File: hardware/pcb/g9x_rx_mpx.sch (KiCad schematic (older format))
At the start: 31 parts, among them IC1 ATMEGA328-M, K1 CONN_3, K2 CONN_3, K3 CONN_3, P1 CONN_3X2, P2 CONN_8X3, P3 CONN_8X2, SW1 SPDT_SW, SW2 SPDT_SW, U1 7805, U2 ULN2803, U3 4017_GRUVIN

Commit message: Couple of pin changes to the Rx deMUX board
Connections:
- wire segments 180 -> 178
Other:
- moved on the sheet: C1, C2, C3, C4, C5, C6, C7, C8, C9, IC1, K1, K2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

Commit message: Rx DEMUX board getting closer . Tidied up the schematic . Added fuses . Via-ed the GND pours . Tidied the silkscreen . Also have some working code for testing the hardware PPM decode and encode
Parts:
- added F1, F2: FUSE, symbol FUSE
- added P4: CONN_4, symbol CONN_4
- added P5, P6: CONN_1, symbol CONN_1
- added R11: 4.7k, symbol R
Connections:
- net labels added: RXD, TXD
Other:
- moved on the sheet: P3, U2

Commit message: Rx MPX - Changed switch types (cheaper and better spec), moved fuses. Still want to add a couple of dip switches and an LED for user config options. Then it's done.
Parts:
- removed SW1, SW2: SPDT_SW, symbol SPDT_SW
- added SW1, SW2: SPDT_SW_PCB, symbol SPDT_SW_PCB
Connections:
- wire segments 178 -> 184
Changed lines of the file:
@@
-EESchema Schematic File Version 2  date 02/11/2011 19:17:17
+EESchema Schematic File Version 2  date 15/02/2012 11:27:38
 LIBS:device
 LIBS:transistors
@@
 Sheet 1 1
 Title "G9X Rx Multiplexer Board"
-Date "2 nov 2011"
+Date "15 feb 2012"
 Rev "1.0"
 Comp "gruvin9x"
@@
 Comment4 "Licensed under the TAPR Open Hardware License (see file,  LICENSE)"
 $EndDescr
+Connection ~ 10050 9350
+Wire Wire Line
+	10050 9550 10050 9150
+Wire Wire Line
+	10050 9150 10200 9150
+Connection ~ 9950 2200
+Wire Wire Line
+	10100 2000 9950 2000
+Wire Wire Line
+	9950 2000 9950 2350
 Connection ~ 7750 5450
 Wire Wire Line
@@
 Wire Wire Line
 	7750 4300 7750 4800
+Wire Wire Line
+	9950 2200 10100 2200
+Wire Wire Line
+	10050 9350 10200 9350
+$Comp
+L GND #PWR?
+U 1 1 4F3B9583
+P 10050 9550
+F 0 "#PWR?" H 10050 9550 30  0001 C CNN
+F 1 "GND" H 10050 9480 30  0001 C CNN
+	1    10050 9550
+	1    0    0    -1
+$EndComp
+$Comp
+L GND #PWR?
+U 1 1 4F3B9567
+P 9950 2350
+F 0 "#PWR?" H 9950 2350 30  0001 C CNN
+F 1 "GND" H 9950 2280 30  0001 C CNN
+	1    9950 2350
+	1    0    0    -1
+$EndComp
+$Comp
+L SPDT_SW_PCB SW2
+U 1 1 4F3B8BE9
+P 10700 9050
+F 0 "SW2" H 10500 9400 50  0000 C CNN
+F 1 "SPDT_SW_PCB" H 11000 9500 50  0000 C CNN
+	1    10700 9050
+	-1   0    0    -1
+$EndComp
+$Comp
+L SPDT_SW_PCB SW1
+U 1 1 4F3B8BE1
+P 10600 1900
+F 0 "SW1" H 10400 2250 50  0000 C CNN
+F 1 "SPDT_SW_PCB" H 10900 2350 50  0000 C CNN
+	1    10600 1900
+	-1   0    0    -1
+$EndComp
 $Comp
 L R R11
@@
 Text Label 11050 9450 0    60   ~ 0
 AUX_BATT_2
-Text Label 9750 8750 0    60   ~ 0
+Text Label 9750 8950 0    60   ~ 0
 AUX_BATT_2
 Text Label 9600 1600 0    60   ~ 0
@@
 Text Label 7150 2800 0    60   ~ 0
 SPI_MISO
-Text Label 9750 8950 0    60   ~ 0
+Text Label 9750 8750 0    60   ~ 0
 BATT_RX
 Text Label 9600 1800 0    60   ~ 0
 BATT_RX
 $Comp
-L SPDT_SW SW2
-U 1 1 4EA0A57B
-P 10700 8650
-F 0 "SW2" H 10500 9000 50  0000 C CNN
-F 1 "SPDT_SW" H 11000 9100 50  0000 C CNN
-	1    10700 8650
-	-1   0    0    1
-$EndComp
-$Comp
-L SPDT_SW SW1
-U 1 1 4EA0A572
-P 10600 1900
-F 0 "SW1" H 10400 2250 50  0000 C CNN
-F 1 "SPDT_SW" H 10900 2350 50  0000 C CNN
-	1    10600 1900
-	-1   0    0    -1
-$EndComp
-$Comp
 L CONN_3X2 P1

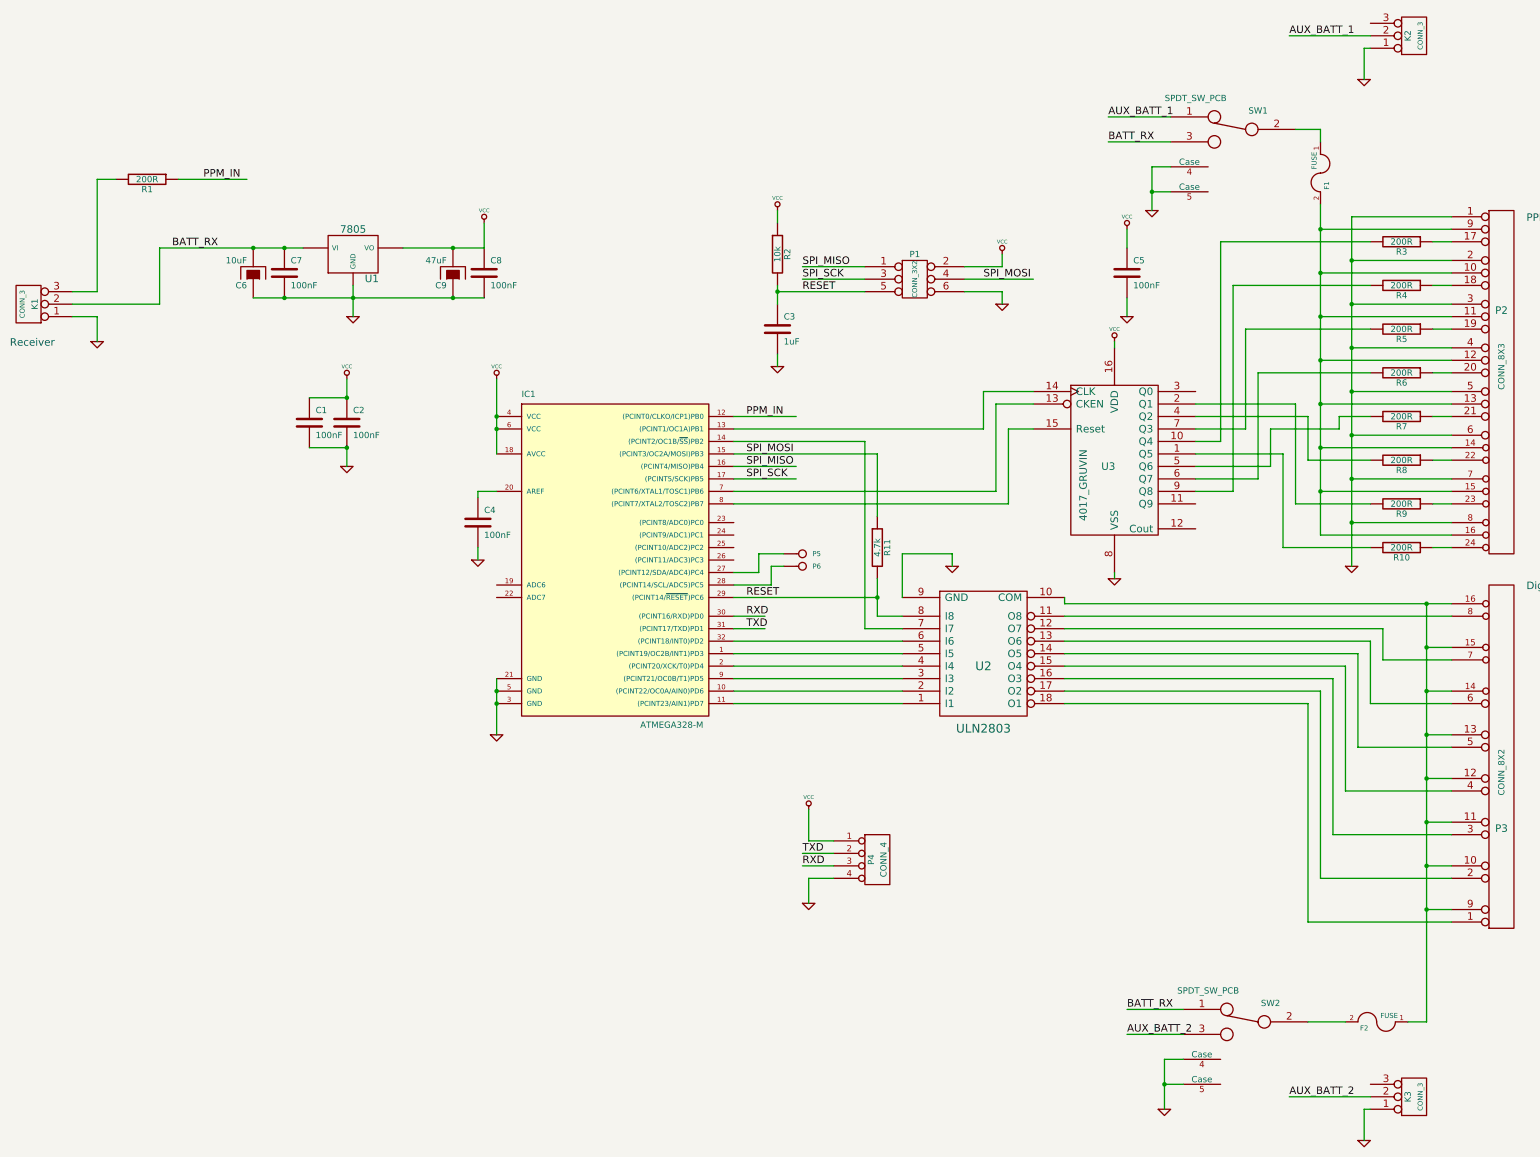
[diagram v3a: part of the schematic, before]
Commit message: Rx MPX board - added LED and dip switches. LED needs attention, no 3D model. Also via search needs to occur.
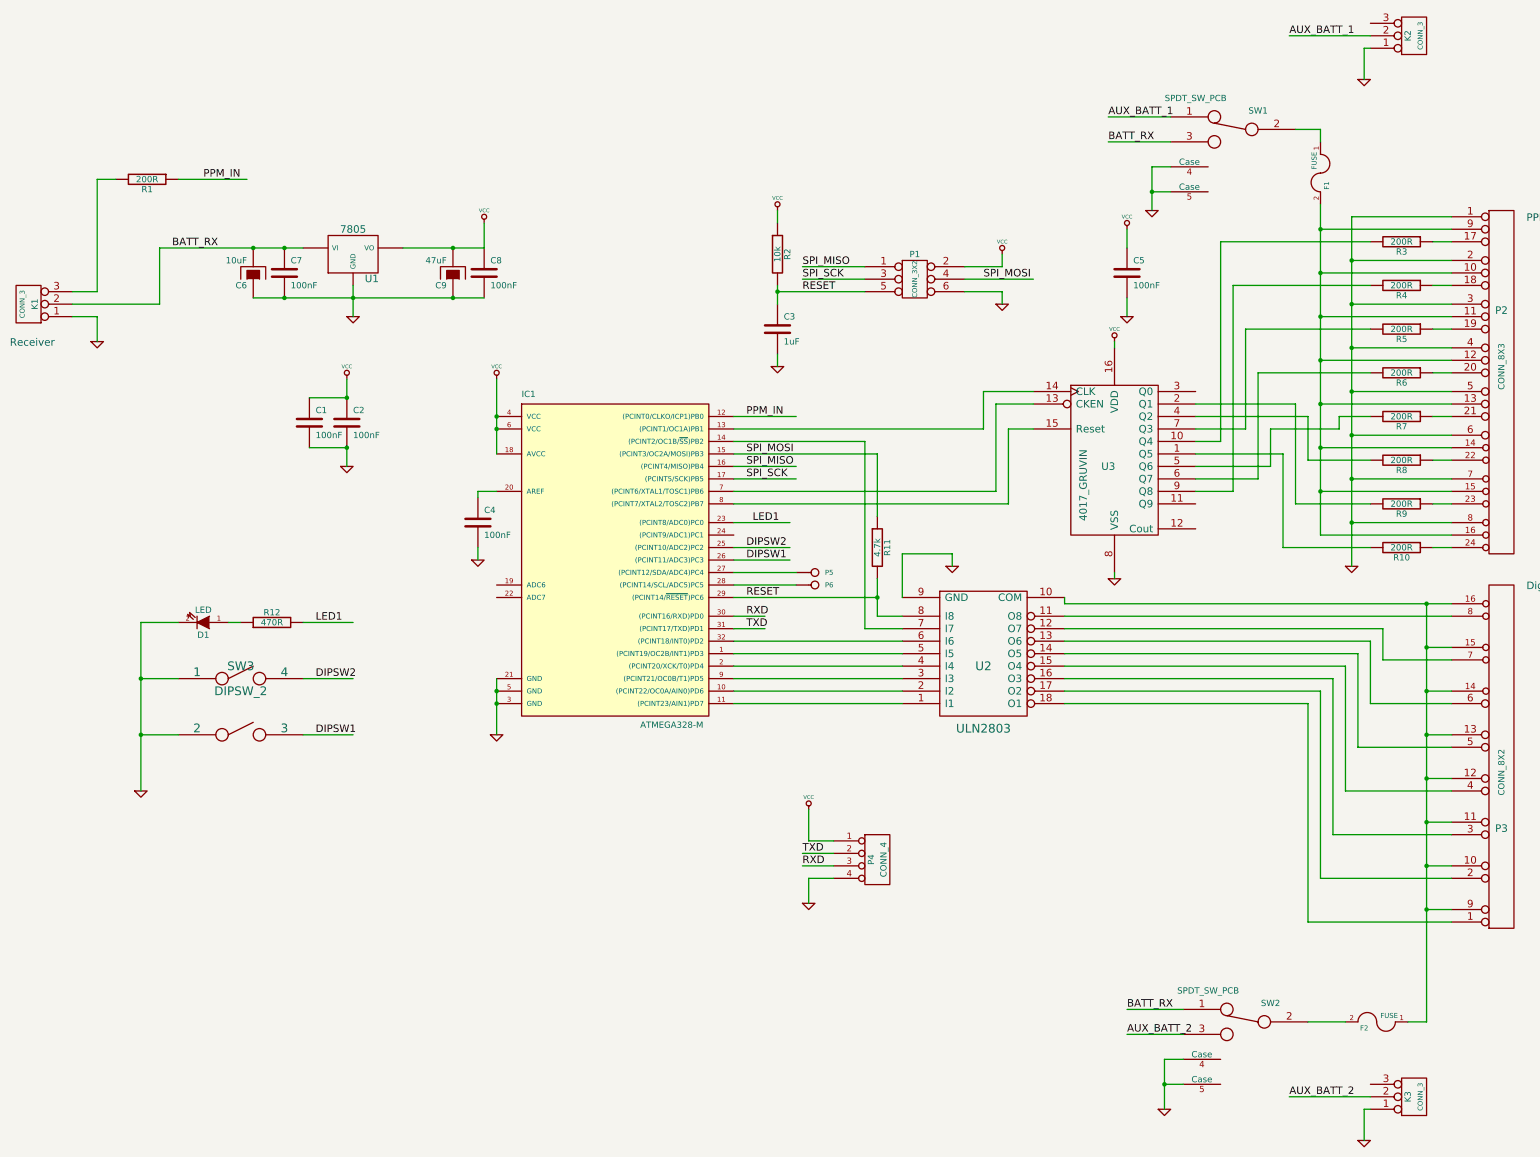
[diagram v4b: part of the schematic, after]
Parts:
- added D1: LED, symbol LED
- added R12: 470R, symbol R
- added SW3: DIPSW_2, symbol DIPSW_2
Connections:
- net labels added: DIPSW1, DIPSW2, LED1
- wire segments 184 -> 191
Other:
- moved on the sheet: P5, P6

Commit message: Rx MPX - Final changes, two regulator alternatives. Next step order them. Bed now, gerbers tomorrow !
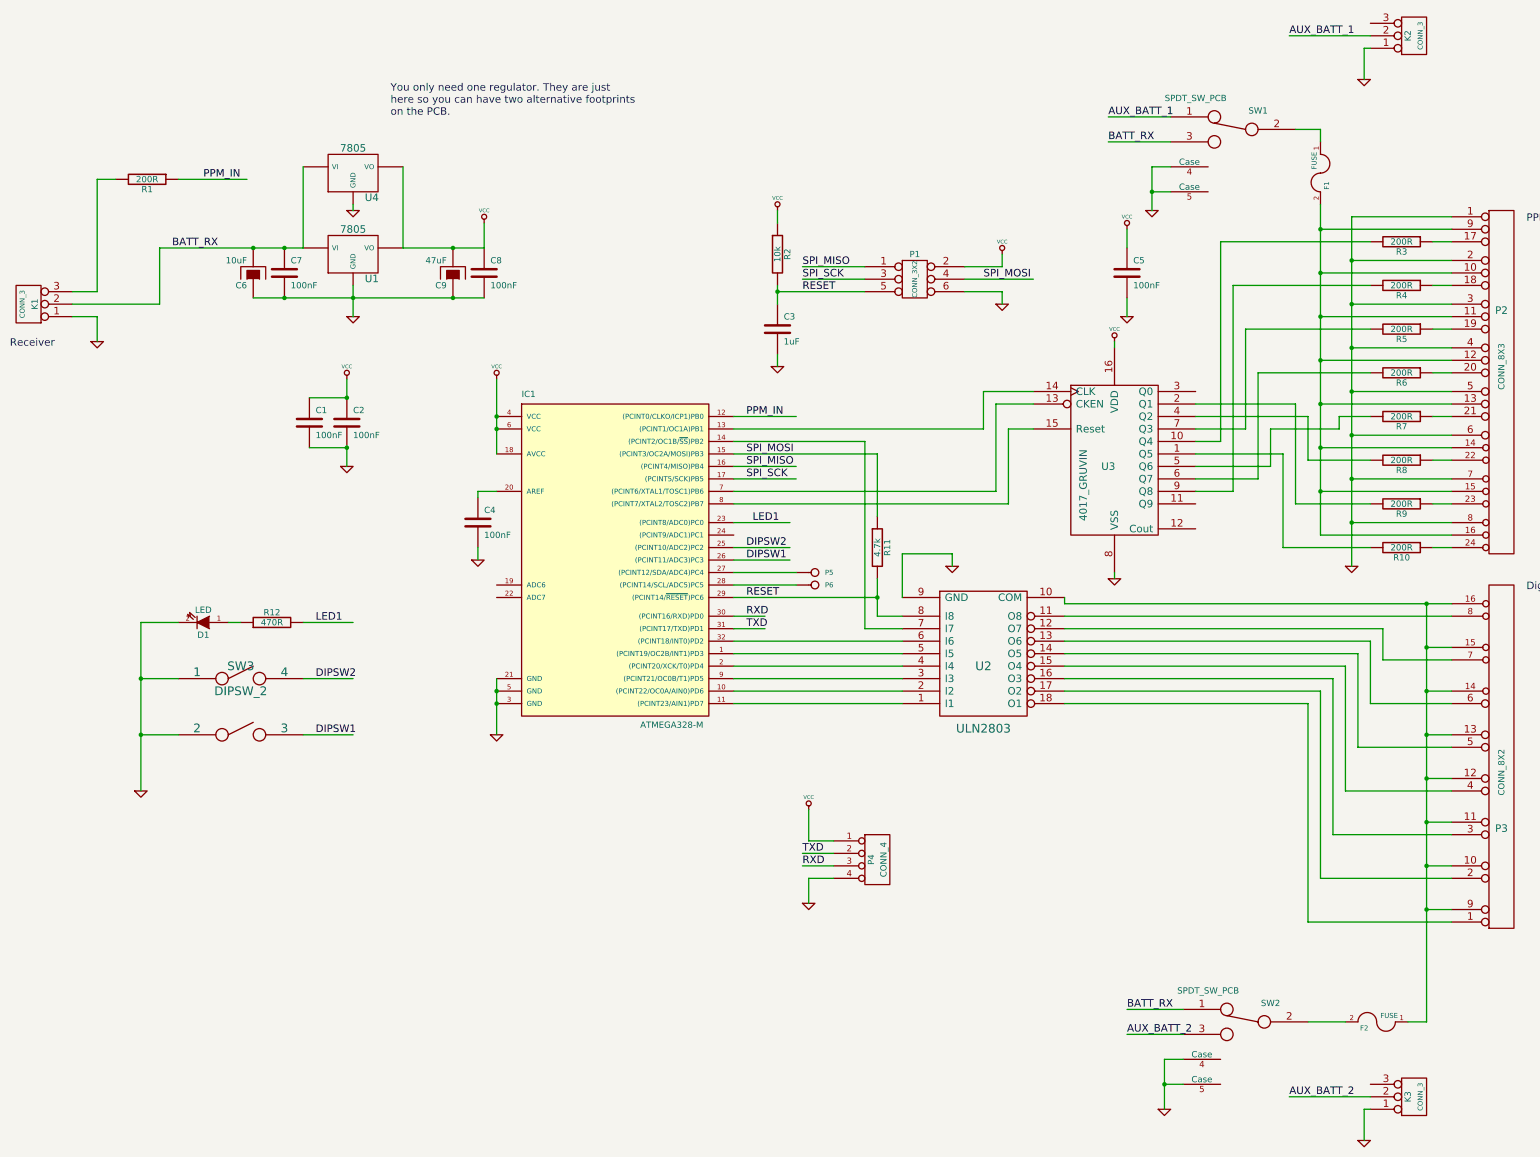
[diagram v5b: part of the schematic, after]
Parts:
- added U4: 7805, symbol 7805
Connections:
- wire segments 191 -> 194
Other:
- note added: "You only need one regulator. They are just\nhere so you can have two alternative footprints\non the PCB."

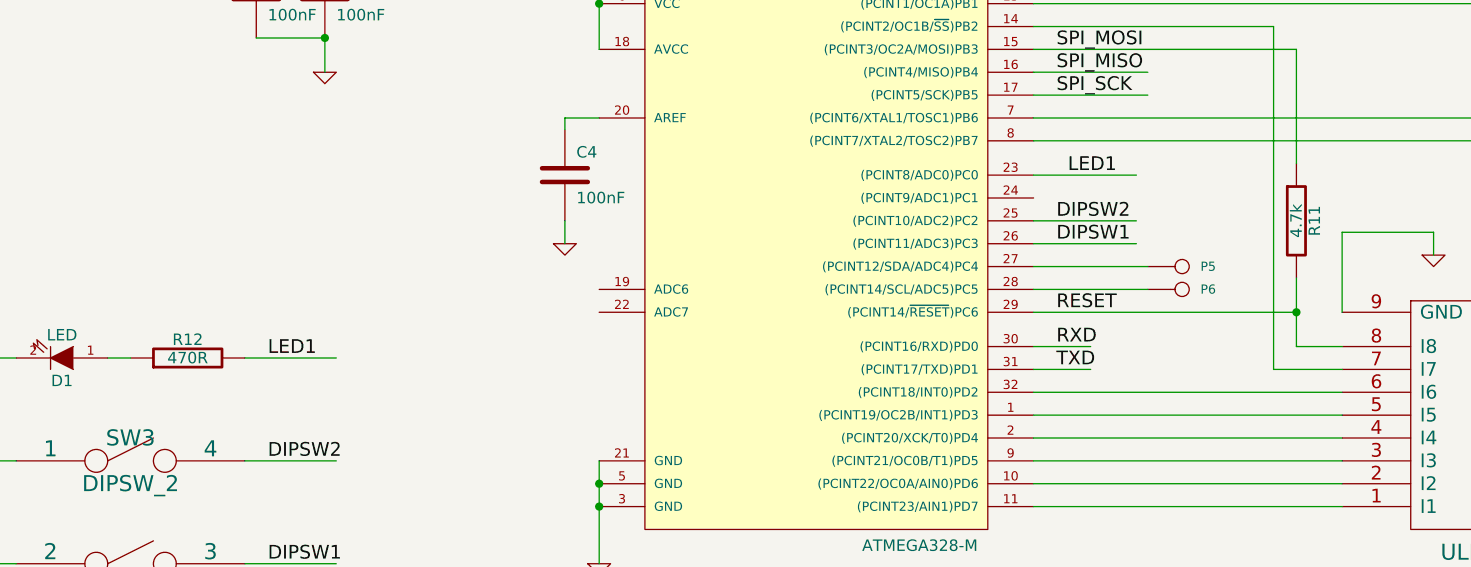
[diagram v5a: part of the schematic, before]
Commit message: RX MPX Board: 1st BOM Plus a change of the fuse footprint, can't get required voltage and current rating in the footprint I used, oops.
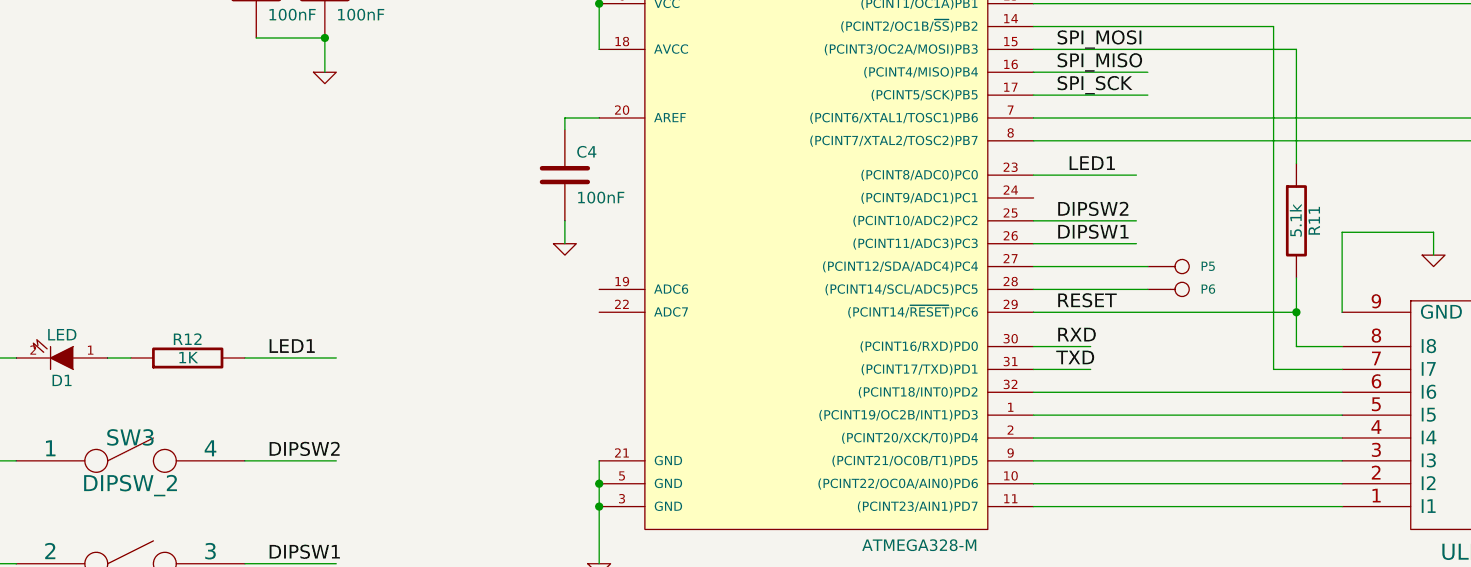
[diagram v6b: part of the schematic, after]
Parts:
- R11: value 4.7k -> 5.1k
- R12: value 470R -> 1K
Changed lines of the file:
@@
-EESchema Schematic File Version 2  date 02/03/2012 00:46:23
+EESchema Schematic File Version 2  date 11/06/2012 23:49:05
 LIBS:device
 LIBS:transistors
@@
 Sheet 1 1
 Title "G9X Rx Multiplexer Board"
-Date "2 mar 2012"
+Date "11 jun 2012"
 Rev "1.0"
 Comp "gruvin9x"
@@
 P 2900 5650
 F 0 "R12" V 2980 5650 50  0000 C CNN
-F 1 "470R" V 2900 5650 50  0000 C CNN
+F 1 "1K" V 2900 5650 50  0000 C CNN
 	1    2900 5650
 	0    -1   -1   0
@@
 P 7750 5050
 F 0 "R11" V 7830 5050 50  0000 C CNN
-F 1 "4.7k" V 7750 5050 50  0000 C CNN
+F 1 "5.1k" V 7750 5050 50  0000 C CNN
 	1    7750 5050
 	1    0    0    -1
